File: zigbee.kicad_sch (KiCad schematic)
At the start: 44 parts, among them J301 Conn_Coaxial, J302 Conn_Coaxial, U301 CC2652P1FRGZR, U302 0900PC15A0036E, X301 Crystal, X302 Crystal_GND24

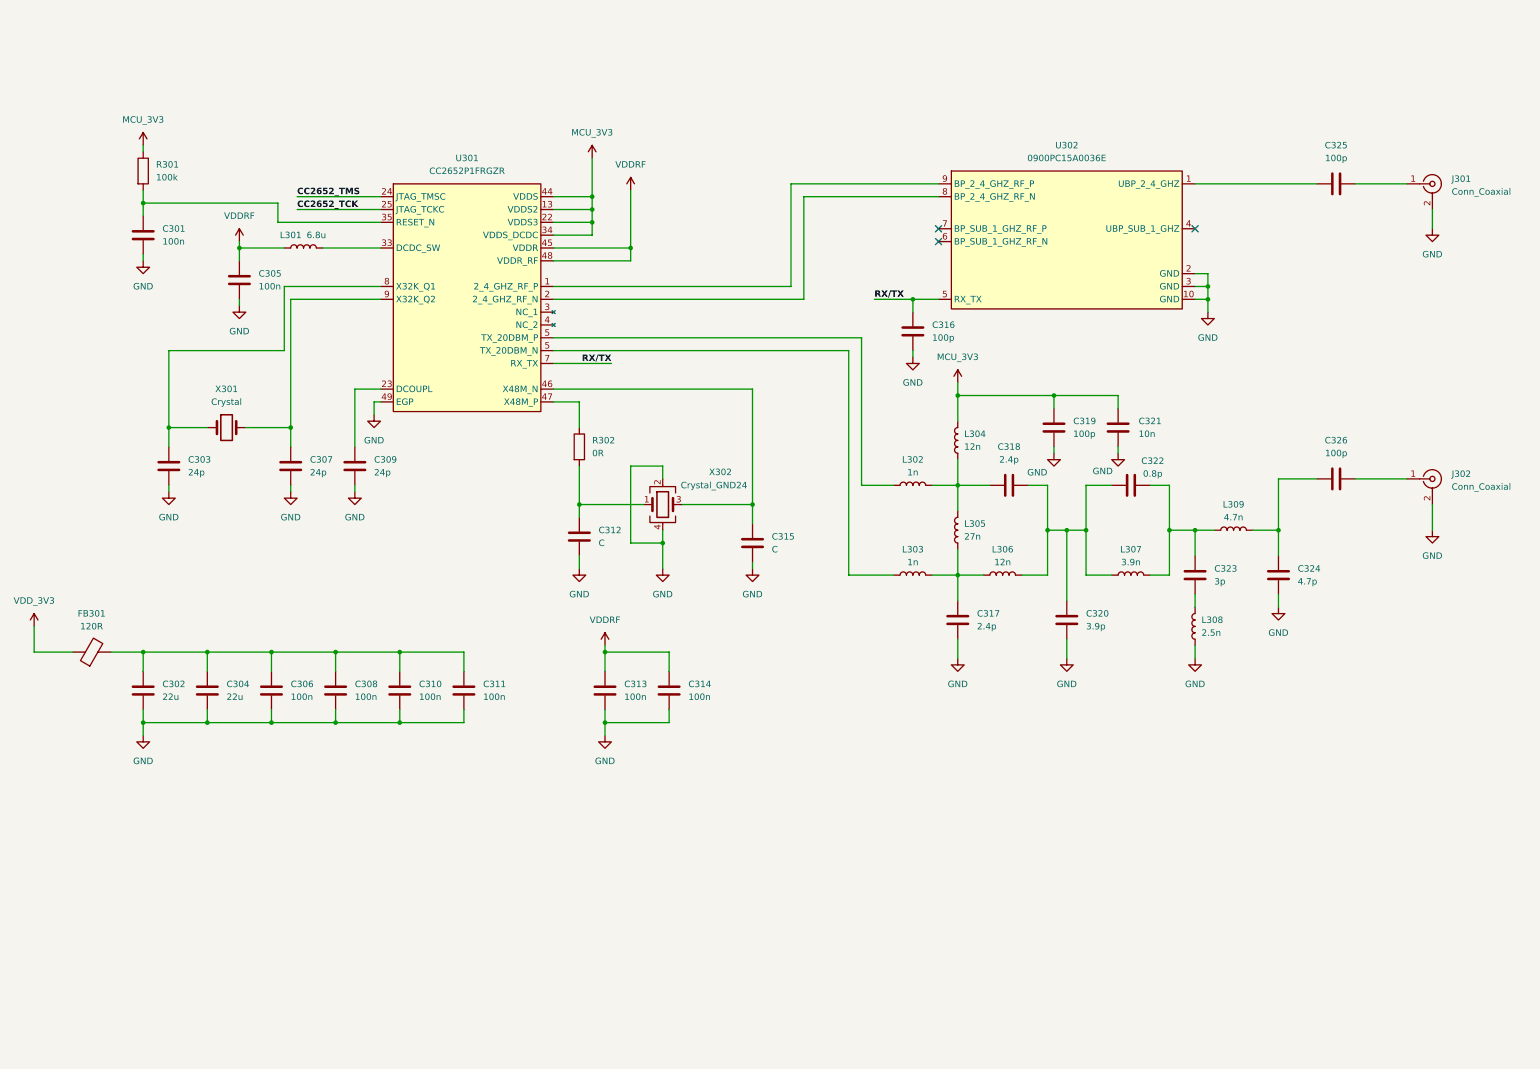
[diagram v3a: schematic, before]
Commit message: Added some net labels and schematic routing
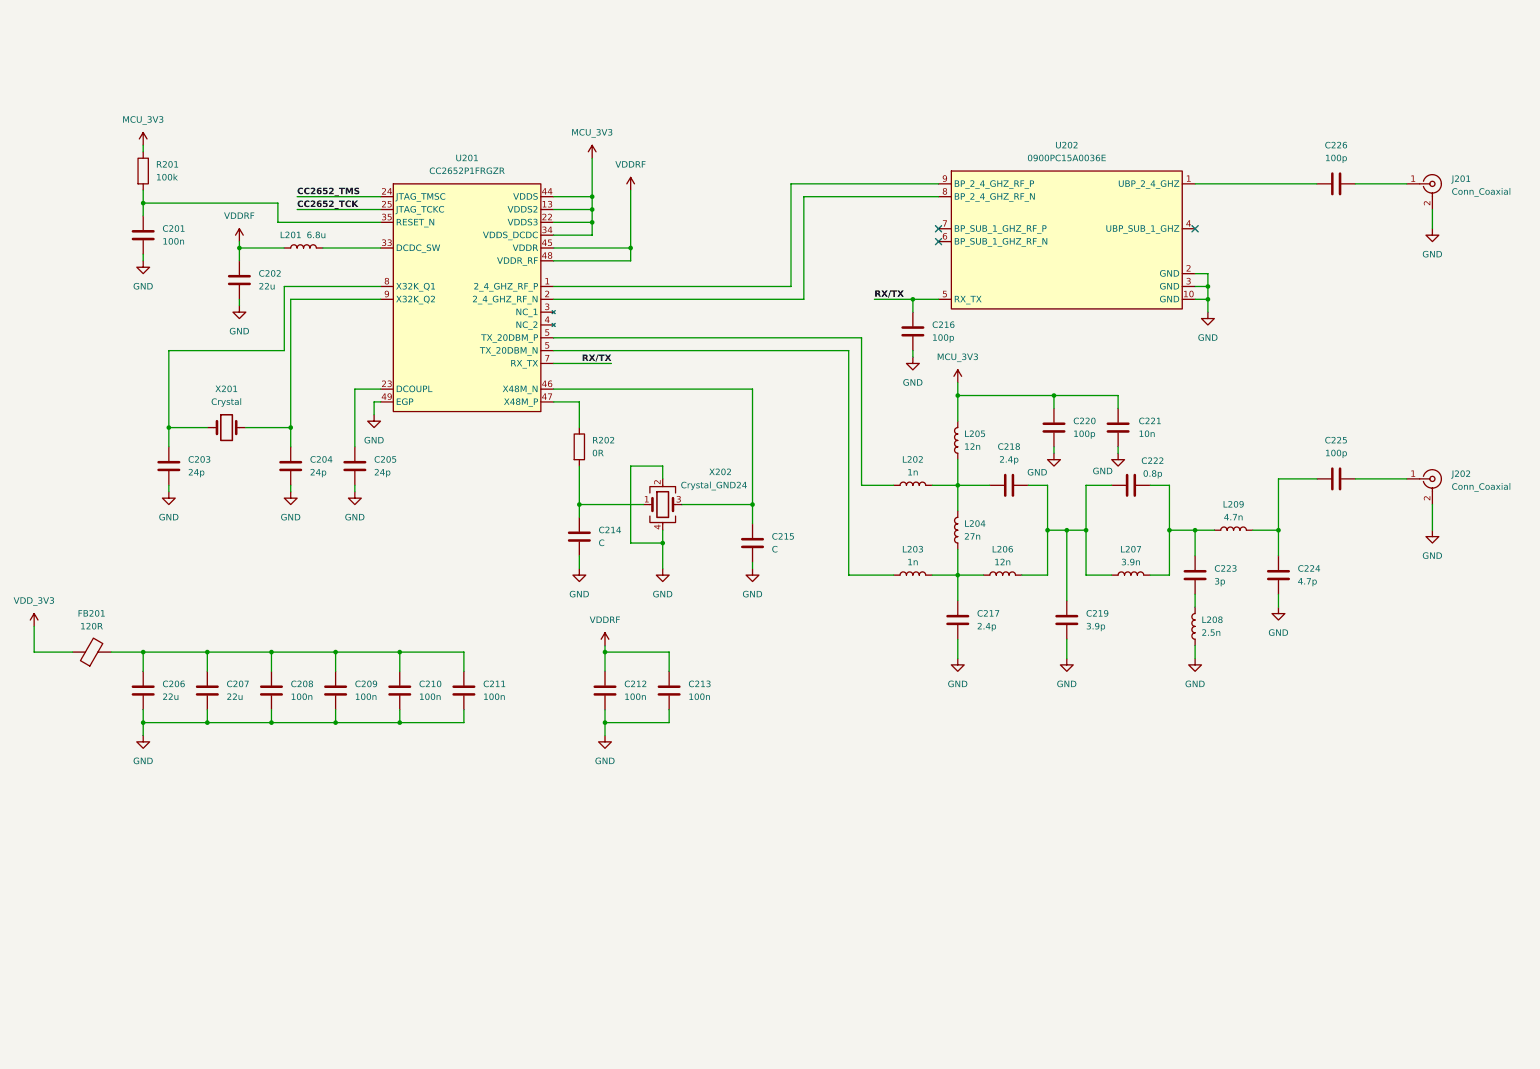
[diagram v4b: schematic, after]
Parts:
- C202: renamed from C305; value 100n -> 22u
- renumbered C301 to C201, C303 to C203, C307 to C204, C309 to C205, C302 to C206, C304 to C207, C306 to C208, C308 to C209, C310 to C210, C311 to C211, C313 to C212, C314 to C213, C312 to C214, C315 to C215, C316 to C216, C317 to C217, C318 to C218, C320 to C219, C319 to C220, C321 to C221, C322 to C222, C323 to C223, C324 to C224, C326 to C225, C325 to C226, FB301 to FB201, J301 to J201, J302 to J202, L301 to L201, L302 to L202, L303 to L203, L305 to L204, L304 to L205, L306 to L206, L307 to L207, L308 to L208, L309 to L209, R301 to R201, R302 to R202, U301 to U201, U302 to U202, X301 to X201, X302 to X202

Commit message: Worked on schematic for DDR4 memory
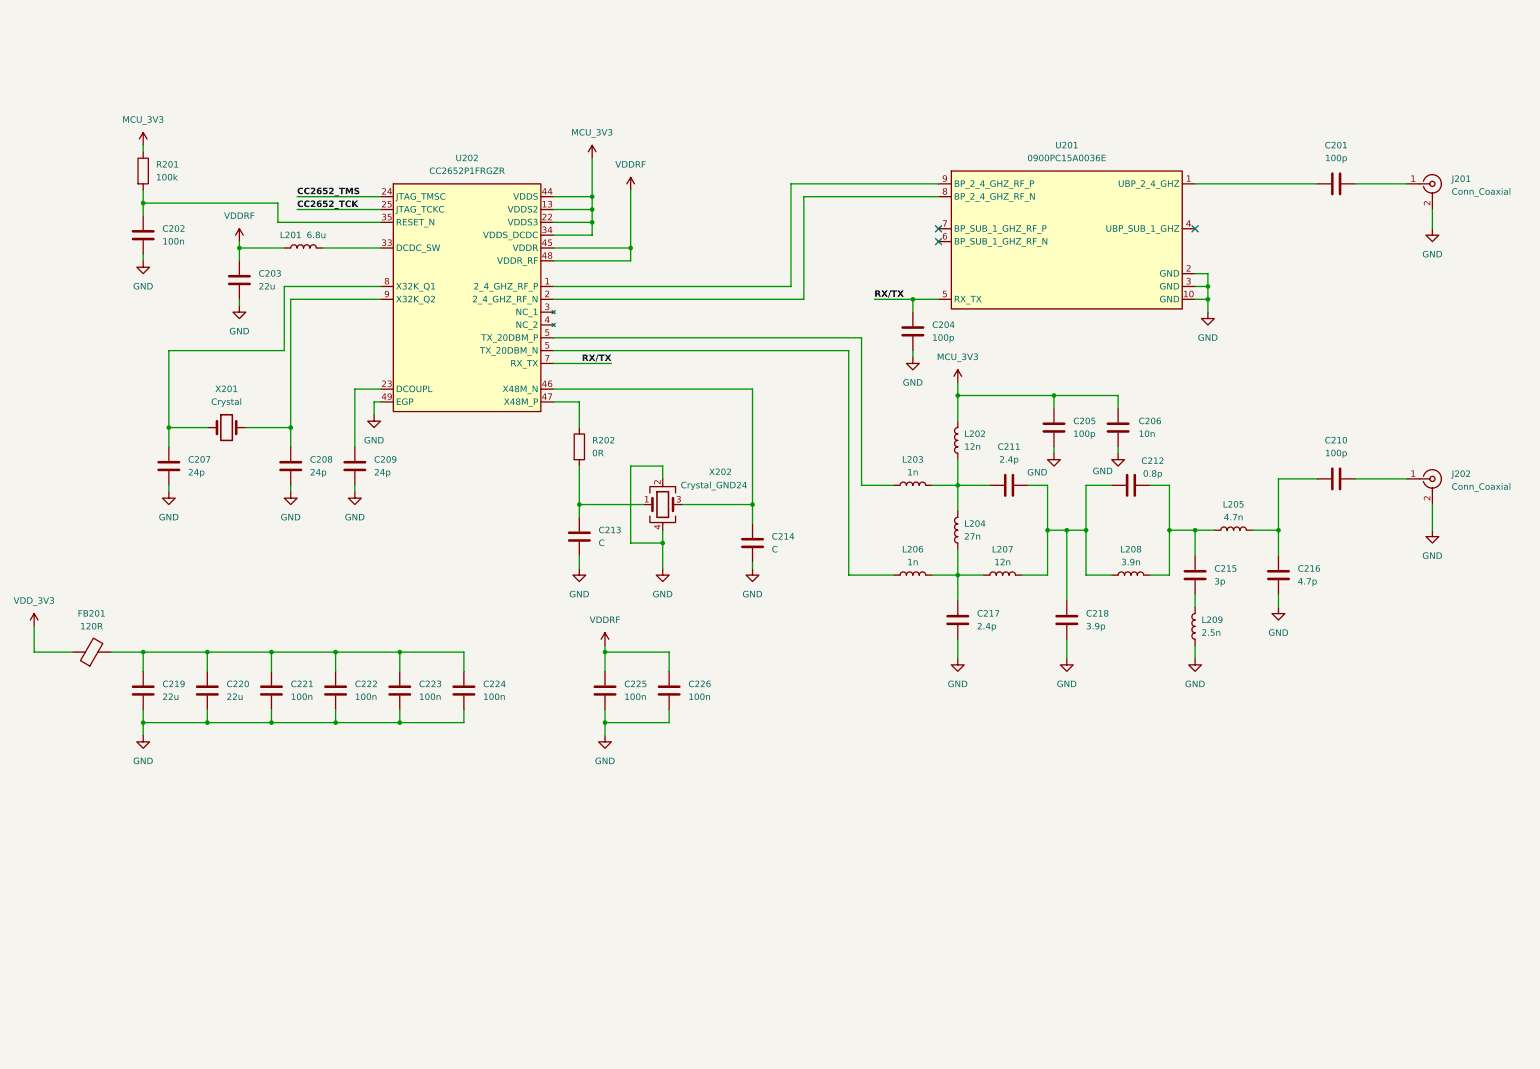
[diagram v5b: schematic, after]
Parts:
- renumbered C226 to C201, C201 to C202, C202 to C203, C216 to C204, C220 to C205, C221 to C206, C203 to C207, C204 to C208, C205 to C209, C225 to C210, C218 to C211, C222 to C212, C214 to C213, C215 to C214, C223 to C215, C224 to C216, C219 to C218, C206 to C219, C207 to C220, C208 to C221, C209 to C222, C210 to C223, C211 to C224, C212 to C225, C213 to C226, L205 to L202, L202 to L203, L209 to L205, L203 to L206, L206 to L207, L207 to L208, L208 to L209, U202 to U201, U201 to U202

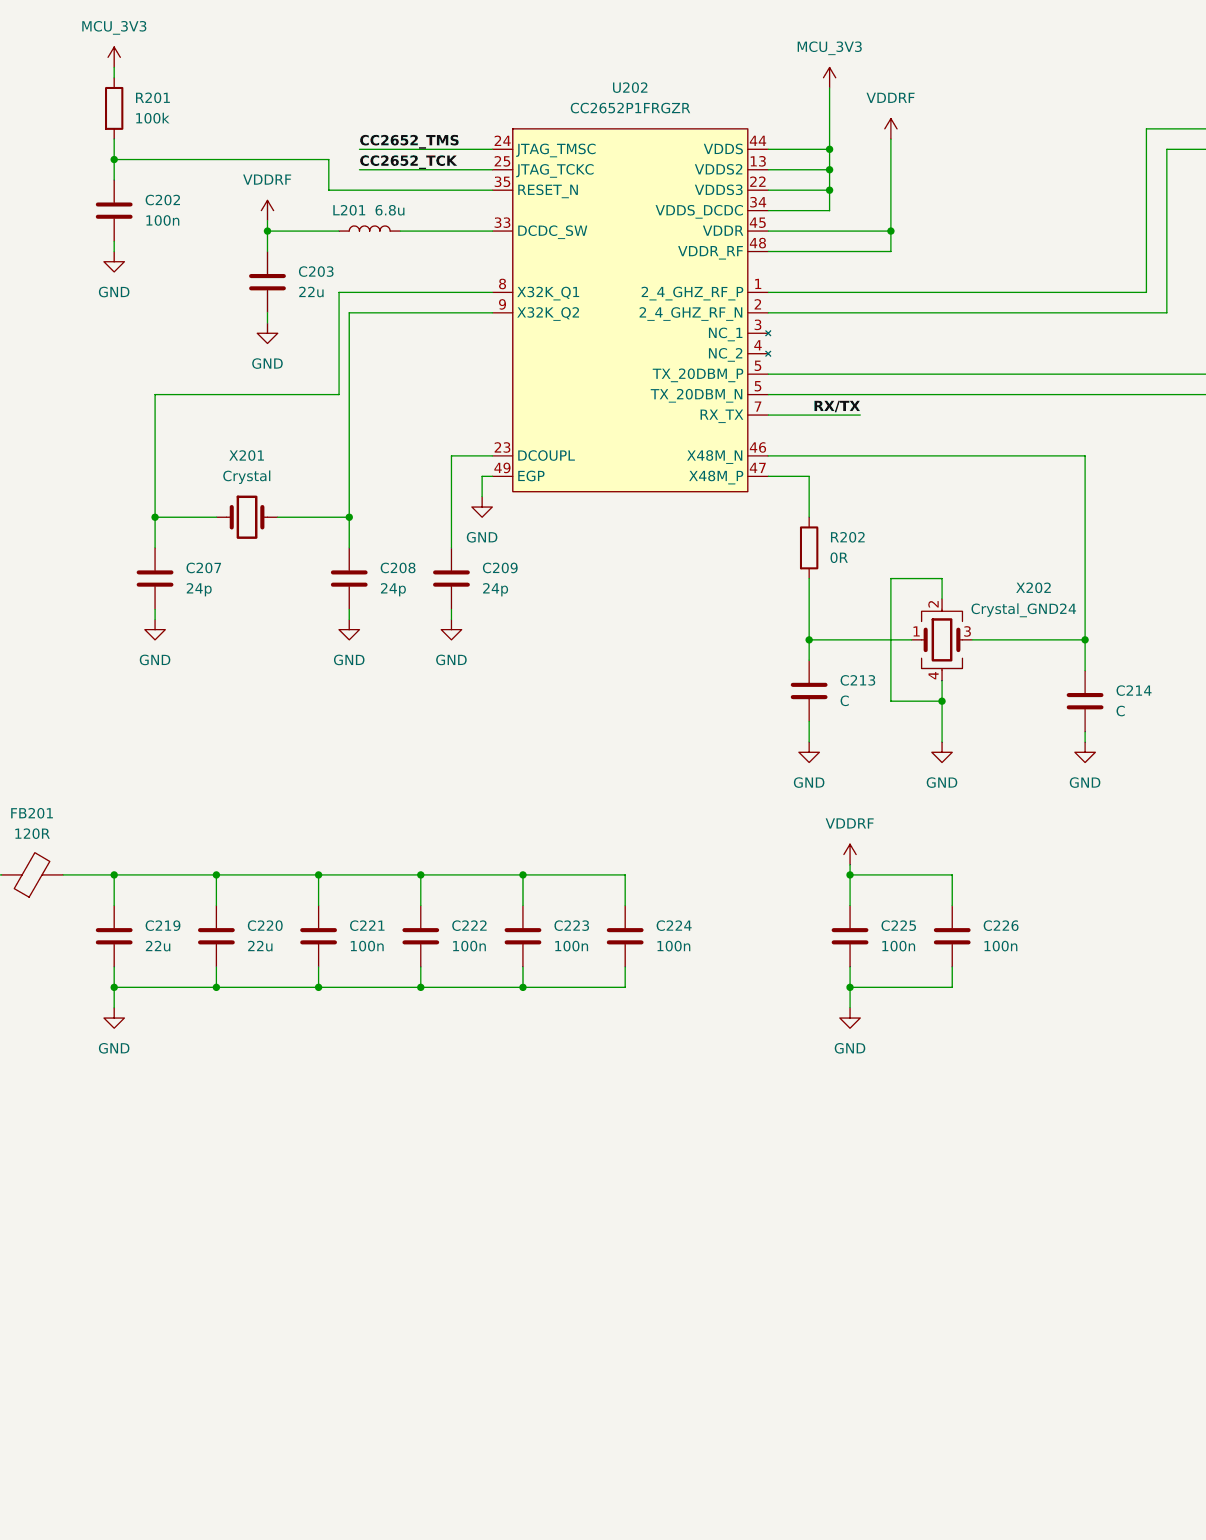
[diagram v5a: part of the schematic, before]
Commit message: Finished CC2652P and UART2
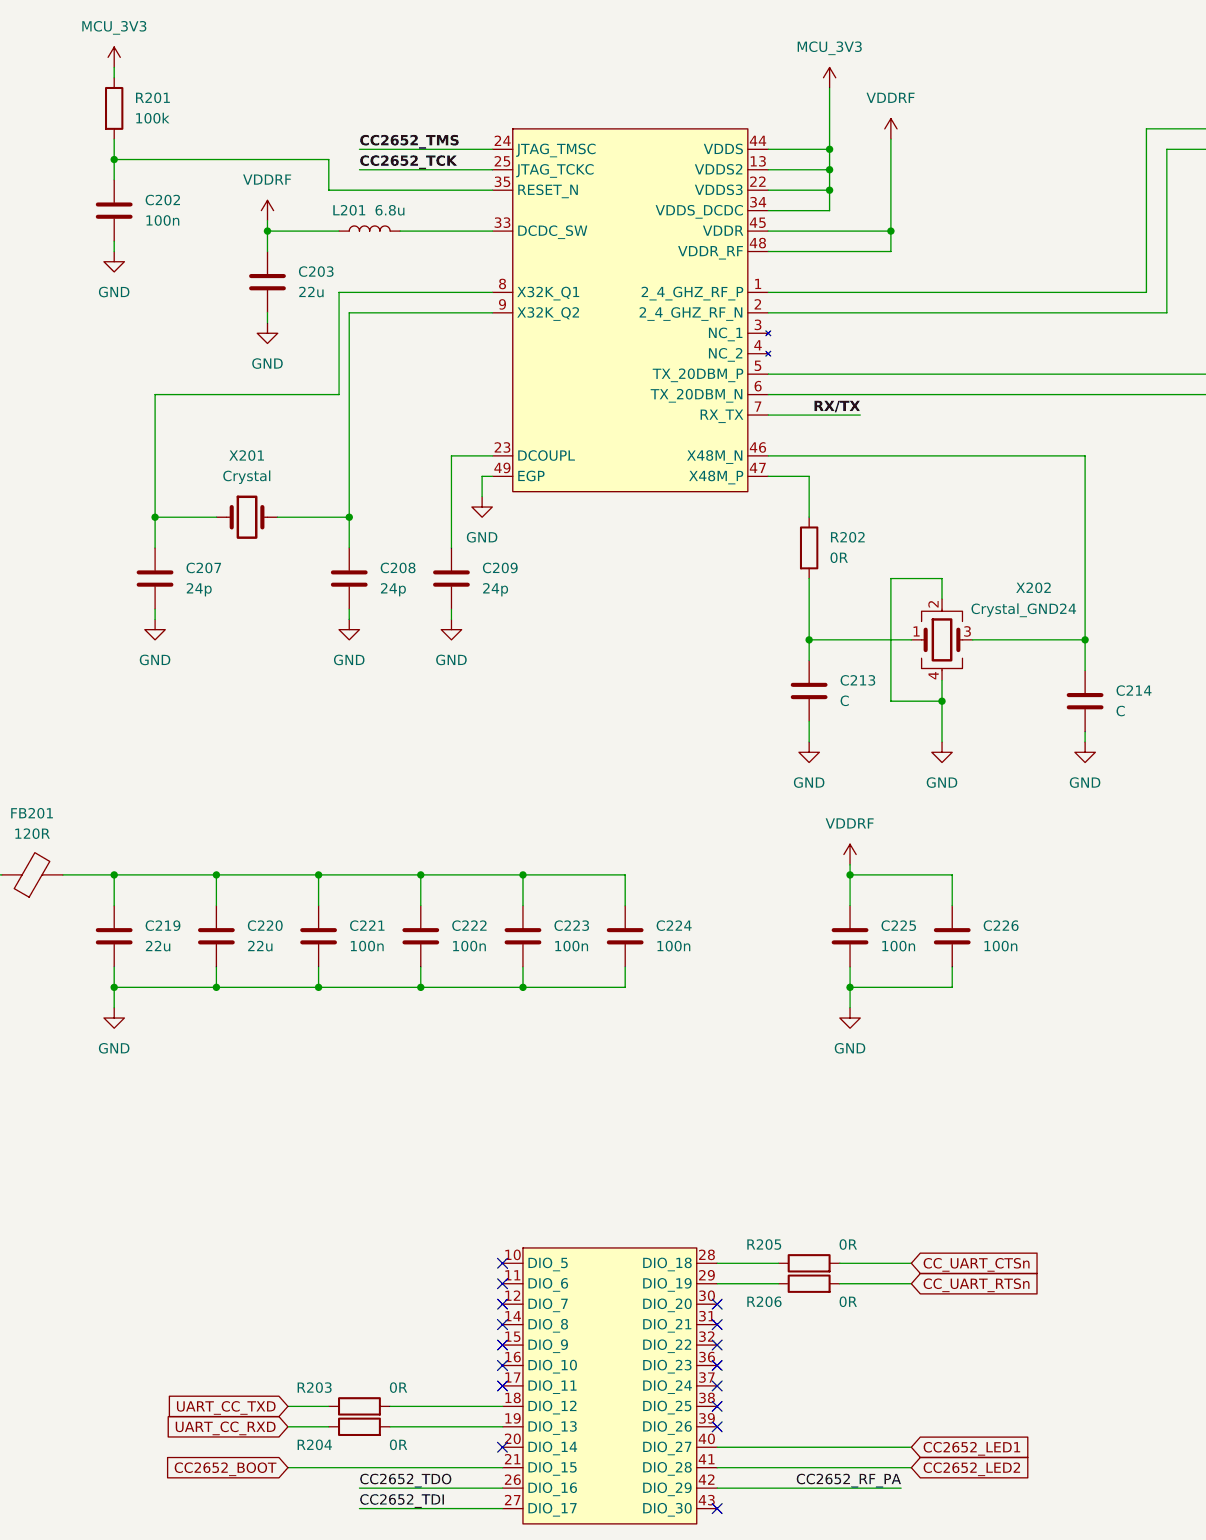
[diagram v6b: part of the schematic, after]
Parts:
- added R203, R204, R205, R206: 0R, symbol Device:R
- added U203: CC2652P1FRGZR, symbol SoftServicesSymbolLibrary:CC2652P1FRGZR
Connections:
- net at L206.1: now also U202.6 (TX_20DBM_N); no longer U202.5 (TX_20DBM_N)
- new net: R203.2, U203.18 (DIO_12)
- new net: R204.2, U203.19 (DIO_13)
- new net: R205.1, U203.28 (DIO_18)
- new net: R206.1, U203.29 (DIO_19)
- new net CC2652_BOOT: U203.21 (DIO_15)
- new net CC2652_LED1: U203.40 (DIO_27)
- new net CC2652_LED2: U203.41 (DIO_28)
- new net CC2652_RF_PA: U203.42 (DIO_29)
- new net CC2652_TDI: U203.27 (DIO_17)
- new net CC2652_TDO: U203.26 (DIO_16)
- new net CC_UART_CTSn: R205.2
- new net CC_UART_RTSn: R206.2
- new net UART_CC_RXD: R204.1
- new net UART_CC_TXD: R203.1
- no-connect marks 3 -> 19

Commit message: Fixed power issues
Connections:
- net UART_CC_RXD renamed CC_UART_RXD
- net UART_CC_TXD renamed CC_UART_TXD
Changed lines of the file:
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@@
 		)
 	)
-	(global_label "UART_CC_RXD"
+	(global_label "CC_UART_RXD"
 		(shape input)
 		(at 76.2 251.46 180)
@@
 		)
 	)
-	(global_label "UART_CC_TXD"
+	(global_label "CC_UART_TXD"
 		(shape input)
 		(at 76.2 248.92 180)
